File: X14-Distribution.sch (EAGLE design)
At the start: 55 parts, among them Q1 310mA/60V/1.6Ω, Q2 IRF1018EPBF, Q3 IRF1018EPBF, Q4 IRF1018EPBF, Q5 TRANSISTOR-FET_DMP2004K, Q6 TRANSISTOR-FET_DMP2004K, Q7 TRANSISTOR-FET_DMP2004K, U1 DIST_OR_CONTROL_ALTMK06A-M, U2 DIST_OR_CONTROL_ALTMK06A-M

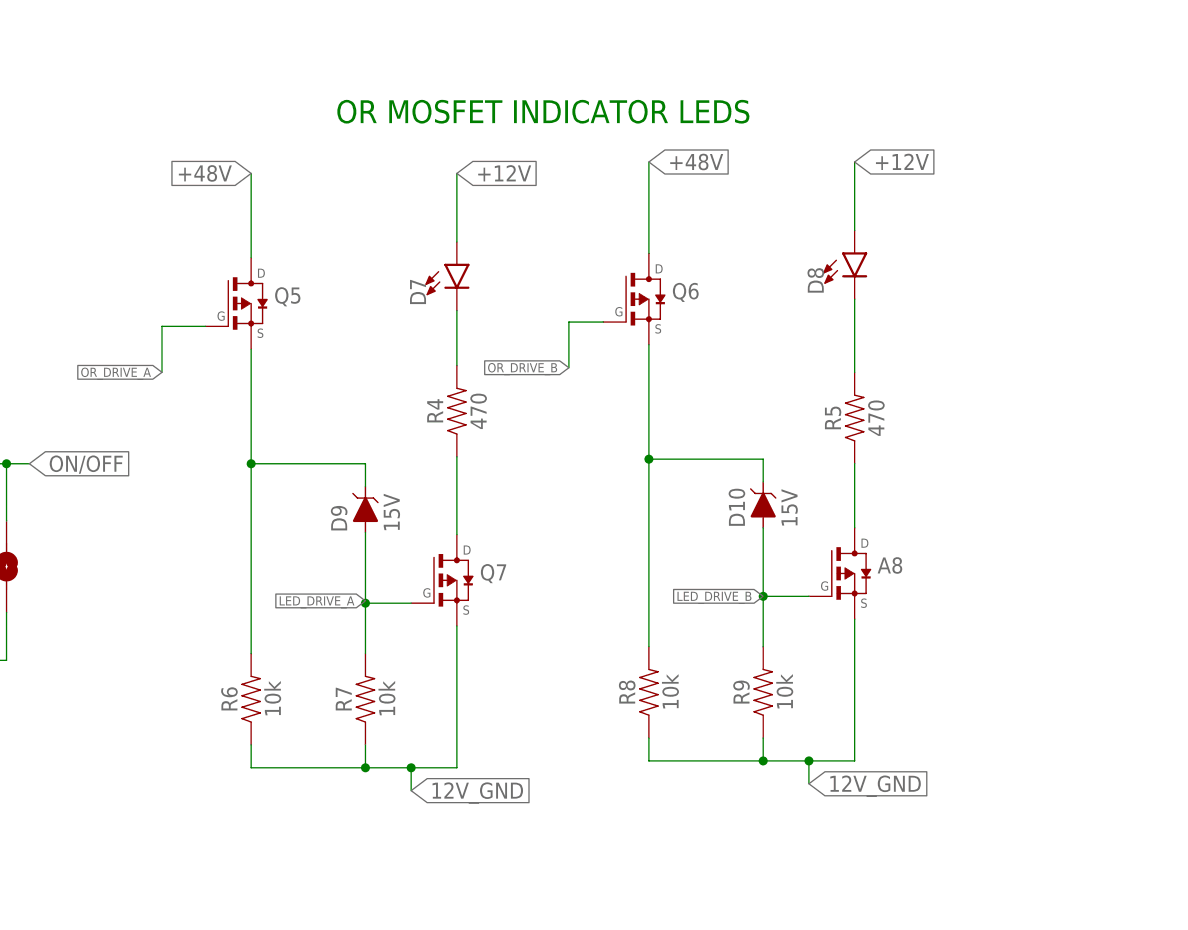
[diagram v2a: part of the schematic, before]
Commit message: Changed the p-mosfets to be oriented the right way
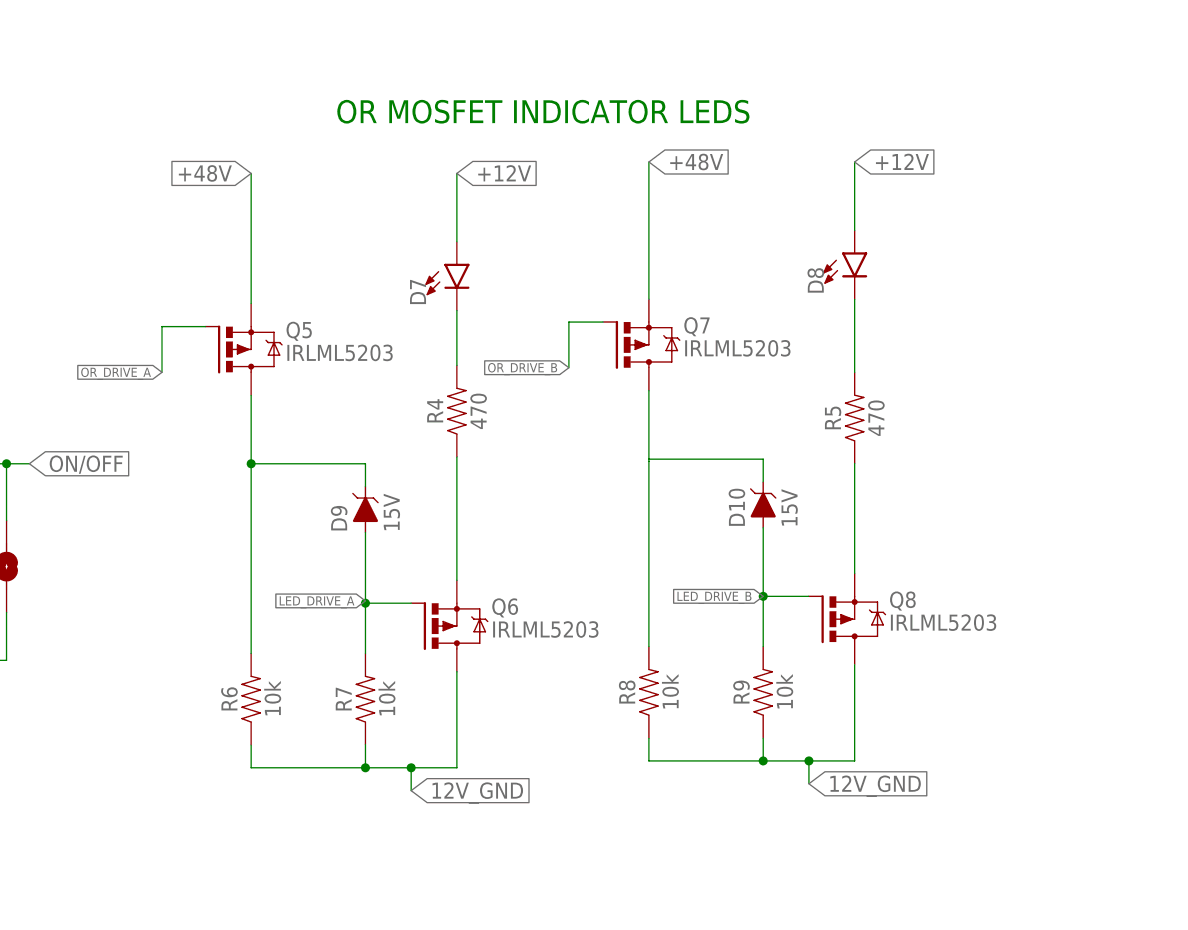
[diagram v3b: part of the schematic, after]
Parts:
- removed A8: TRANSISTOR-FET_DMP2004K, 52101-101-REV-A_v16:TRANSISTOR-FET_DMP2004K
- added Q8: IRLML5203, Transistor:PMOSFET_IRLML5203
- Q5, Q6, Q7: value TRANSISTOR-FET_DMP2004K -> IRLML5203; device 52101-101-REV-A_v16:TRANSISTOR-FET_DMP2004K -> Transistor:PMOSFET_IRLML5203
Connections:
- net +48V: now also Q5.S, Q7.S; no longer Q5.D, Q6.D
- net 12V_GND: now also Q6.D, Q8.D; no longer A8.S, Q7.S
- net LED_DRIVE_A: now also Q6.G; no longer Q7.G
- net LED_DRIVE_B: now also Q8.G; no longer A8.G
- net N$11: now also Q7.D; no longer Q6.S
- net N$3: now also Q6.S; no longer Q7.D
- net N$5: now also Q5.D; no longer Q5.S
- net N$7: now also Q8.S; no longer A8.D
- net OR_DRIVE_B: now also Q7.G; no longer Q6.G
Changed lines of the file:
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@@
 <part name="D11" library="DIODE, Dist Oring Schottky Diode" deviceset="DIODE-DO-214AC(SK34ATR)" device="" value=""/>
 <part name="D12" library="DIODE, Dist Oring Schottky Diode" deviceset="DIODE-DO-214AC(SK34ATR)" device="" value=""/>
-<part name="Q5" library="52101-101-REV-A_v16" library_urn="urn:adsk.eagle:library:21899384" deviceset="TRANSISTOR-FET_DMP2004K" device="" package3d_urn="urn:adsk.eagle:package:15662287/2" value=""/>
-<part name="Q6" library="52101-101-REV-A_v16" library_urn="urn:adsk.eagle:library:21899384" deviceset="TRANSISTOR-FET_DMP2004K" device="" package3d_urn="urn:adsk.eagle:package:15662287/2" value=""/>
-<part name="Q7" library="52101-101-REV-A_v16" library_urn="urn:adsk.eagle:library:21899384" deviceset="TRANSISTOR-FET_DMP2004K" device="" package3d_urn="urn:adsk.eagle:package:15662287/2" value=""/>
-<part name="A8" library="52101-101-REV-A_v16" library_urn="urn:adsk.eagle:library:21899384" deviceset="TRANSISTOR-FET_DMP2004K" device="" package3d_urn="urn:adsk.eagle:package:15662287/2" value=""/>
+<part name="Q5" library="Transistor" library_urn="urn:adsk.eagle:library:16378713" deviceset="PMOSFET_" device="" package3d_urn="urn:adsk.eagle:package:28738/2" technology="IRLML5203" value="IRLML5203"/>
+<part name="Q6" library="Transistor" library_urn="urn:adsk.eagle:library:16378713" deviceset="PMOSFET_" device="" package3d_urn="urn:adsk.eagle:package:28738/2" technology="IRLML5203" value="IRLML5203"/>
+<part name="Q7" library="Transistor" library_urn="urn:adsk.eagle:library:16378713" deviceset="PMOSFET_" device="" package3d_urn="urn:adsk.eagle:package:28738/2" technology="IRLML5203" value="IRLML5203"/>
+<part name="Q8" library="Transistor" library_urn="urn:adsk.eagle:library:16378713" deviceset="PMOSFET_" device="" package3d_urn="urn:adsk.eagle:package:28738/2" technology="IRLML5203" value="IRLML5203"/>
 </parts>
 <sheets>
@@
 <attribute name="VALUE" x="179.07" y="-69.342" size="1.778" layer="96"/>
 </instance>
-<instance part="Q5" gate="G$1" x="190.246" y="116.3574" smashed="yes">
-<attribute name="VALUE" x="192.786" y="113.8174" size="1.778" layer="96"/>
-<attribute name="NAME" x="192.786" y="116.3574" size="1.778" layer="95"/>
-</instance>
-<instance part="Q6" gate="G$1" x="234.442" y="116.84" smashed="yes">
-<attribute name="VALUE" x="236.982" y="114.3" size="1.778" layer="96"/>
-<attribute name="NAME" x="236.982" y="116.84" size="1.778" layer="95"/>
-</instance>
-<instance part="Q7" gate="G$1" x="213.106" y="85.598" smashed="yes">
-<attribute name="VALUE" x="215.646" y="83.058" size="1.778" layer="96"/>
-<attribute name="NAME" x="215.646" y="85.598" size="1.778" layer="95"/>
-</instance>
-<instance part="A8" gate="G$1" x="257.302" y="86.36" smashed="yes">
-<attribute name="VALUE" x="259.842" y="83.82" size="1.778" layer="96"/>
-<attribute name="NAME" x="259.842" y="86.36" size="1.778" layer="95"/>
+<instance part="Q5" gate="G$1" x="187.706" y="111.252" smashed="yes">
+<attribute name="NAME" x="194.056" y="112.522" size="1.778" layer="95"/>
+<attribute name="VALUE" x="194.056" y="109.982" size="1.778" layer="96"/>
+</instance>
+<instance part="Q6" gate="G$1" x="210.566" y="80.518" smashed="yes">
+<attribute name="NAME" x="216.916" y="81.788" size="1.778" layer="95"/>
+<attribute name="VALUE" x="216.916" y="79.248" size="1.778" layer="96"/>
+</instance>
+<instance part="Q7" gate="G$1" x="231.902" y="111.76" smashed="yes">
+<attribute name="NAME" x="238.252" y="113.03" size="1.778" layer="95"/>
+<attribute name="VALUE" x="238.252" y="110.49" size="1.778" layer="96"/>
+</instance>
+<instance part="Q8" gate="G$1" x="254.762" y="81.28" smashed="yes">
+<attribute name="NAME" x="261.112" y="82.55" size="1.778" layer="95"/>
+<attribute name="VALUE" x="261.112" y="80.01" size="1.778" layer="96"/>
 </instance>
 </instances>
@@
 </segment>
 <segment>
-<wire x1="190.246" y1="121.4374" x2="190.246" y2="130.81" width="0.1524" layer="91"/>
 <label x="190.246" y="130.81" size="1.778" layer="95" rot="MR0" xref="yes"/>
-<pinref part="Q5" gate="G$1" pin="D"/>
-</segment>
-<segment>
-<wire x1="234.442" y1="121.92" x2="234.442" y2="132.08" width="0.1524" layer="91"/>
+<pinref part="Q5" gate="G$1" pin="S"/>
+<wire x1="190.246" y1="116.332" x2="190.246" y2="130.81" width="0.1524" layer="91"/>
+</segment>
+<segment>
 <label x="234.442" y="132.08" size="1.778" layer="95" xref="yes"/>
-<pinref part="Q6" gate="G$1" pin="D"/>
+<pinref part="Q7" gate="G$1" pin="S"/>
+<wire x1="234.442" y1="116.84" x2="234.442" y2="132.08" width="0.1524" layer="91"/>
 </segment>
 <segment>
@@
 </segment>
 <segment>
-<wire x1="180.34" y1="113.8174" x2="180.34" y2="108.712" width="0.1524" layer="91"/>
 <label x="180.34" y="108.712" size="1.016" layer="95" rot="R180" xref="yes"/>
 <pinref part="Q5" gate="G$1" pin="G"/>
-<wire x1="180.34" y1="113.8174" x2="185.166" y2="113.8174" width="0.1524" layer="91"/>
+<wire x1="180.34" y1="113.792" x2="180.34" y2="108.712" width="0.1524" layer="91"/>
+<wire x1="180.34" y1="113.792" x2="185.166" y2="113.792" width="0.1524" layer="91"/>
 </segment>
 </net>
@@
 <wire x1="225.552" y1="114.3" x2="225.552" y2="109.22" width="0.1524" layer="91"/>
 <label x="225.552" y="109.22" size="1.016" layer="95" rot="R180" xref="yes"/>
-<pinref part="Q6" gate="G$1" pin="G"/>
+<pinref part="Q7" gate="G$1" pin="G"/>
 <wire x1="225.552" y1="114.3" x2="229.362" y2="114.3" width="0.1524" layer="91"/>
 </segment>
@@
 <junction x="208.026" y="64.77"/>
 <label x="208.026" y="62.23" size="1.778" layer="95" xref="yes"/>
-<pinref part="Q7" gate="G$1" pin="S"/>
-<wire x1="213.106" y1="64.77" x2="213.106" y2="80.518" width="0.1524" layer="91"/>
+<pinref part="Q6" gate="G$1" pin="D"/>
+<wire x1="213.106" y1="64.77" x2="213.106" y2="75.438" width="0.1524" layer="91"/>
 </segment>
 <segment>
@@
 <junction x="252.222" y="65.532"/>
 <label x="252.222" y="62.992" size="1.778" layer="95" xref="yes"/>
-<pinref part="A8" gate="G$1" pin="S"/>
-<wire x1="257.302" y1="65.532" x2="257.302" y2="81.28" width="0.1524" layer="91"/>
+<pinref part="Q8" gate="G$1" pin="D"/>
+<wire x1="257.302" y1="65.532" x2="257.302" y2="76.2" width="0.1524" layer="91"/>
 </segment>
 <segment>
@@
 <wire x1="202.946" y1="96.012" x2="202.946" y2="98.552" width="0.1524" layer="91"/>
 <wire x1="202.946" y1="98.552" x2="190.246" y2="98.552" width="0.1524" layer="91"/>
-<pinref part="Q5" gate="G$1" pin="S"/>
-<wire x1="190.246" y1="111.2774" x2="190.246" y2="98.552" width="0.1524" layer="91"/>
 <junction x="190.246" y="98.552"/>
+<pinref part="Q5" gate="G$1" pin="D"/>
+<wire x1="190.246" y1="106.172" x2="190.246" y2="98.552" width="0.1524" layer="91"/>
 </segment>
 </net>
@@
 <label x="202.946" y="83.312" size="1.016" layer="95" rot="R180" xref="yes"/>
 <wire x1="202.946" y1="77.47" x2="202.946" y2="83.058" width="0.1524" layer="91"/>
-<pinref part="Q7" gate="G$1" pin="G"/>
 <wire x1="202.946" y1="83.058" x2="202.946" y2="90.932" width="0.1524" layer="91"/>
 <wire x1="202.946" y1="83.058" x2="208.026" y2="83.058" width="0.1524" layer="91"/>
 <junction x="202.946" y="83.058"/>
+<pinref part="Q6" gate="G$1" pin="G"/>
 </segment>
 </net>
@@
 <pinref part="R8" gate="G$1" pin="2"/>
 <pinref part="D10" gate="G$1" pin="C"/>
-<wire x1="234.442" y1="99.06" x2="234.442" y2="78.232" width="0.1524" layer="91"/>
+<wire x1="234.442" y1="99.06" x2="234.442" y2="98.806" width="0.1524" layer="91"/>
+<wire x1="234.442" y1="98.806" x2="234.442" y2="78.232" width="0.1524" layer="91"/>
 <wire x1="247.142" y1="96.52" x2="247.142" y2="99.06" width="0.1524" layer="91"/>
 <wire x1="247.142" y1="99.06" x2="234.442" y2="99.06" width="0.1524" layer="91"/>
-<pinref part="Q6" gate="G$1" pin="S"/>
-<wire x1="234.442" y1="99.06" x2="234.442" y2="111.76" width="0.1524" layer="91"/>
-<junction x="234.442" y="99.06"/>
+<pinref part="Q7" gate="G$1" pin="D"/>
+<wire x1="234.442" y1="99.06" x2="234.442" y2="106.68" width="0.1524" layer="91"/>
 </segment>
 </net>
@@
 <pinref part="R9" gate="G$1" pin="2"/>
 <pinref part="D10" gate="G$1" pin="A"/>
+<label x="247.142" y="83.82" size="1.016" layer="95" rot="R180" xref="yes"/>
 <wire x1="247.142" y1="78.232" x2="247.142" y2="83.82" width="0.1524" layer="91"/>
-<label x="247.142" y="83.82" size="1.016" layer="95" rot="R180" xref="yes"/>
-<pinref part="A8" gate="G$1" pin="G"/>
+<pinref part="Q8" gate="G$1" pin="G"/>
 <wire x1="247.142" y1="83.82" x2="247.142" y2="91.44" width="0.1524" layer="91"/>
 <wire x1="247.142" y1="83.82" x2="252.222" y2="83.82" width="0.1524" layer="91"/>
@@
 <segment>
 <pinref part="R4" gate="G$1" pin="1"/>
-<pinref part="Q7" gate="G$1" pin="D"/>
-<wire x1="213.106" y1="99.314" x2="213.106" y2="90.678" width="0.1524" layer="91"/>
+<pinref part="Q6" gate="G$1" pin="S"/>
+<wire x1="213.106" y1="99.314" x2="213.106" y2="85.598" width="0.1524" layer="91"/>
 </segment>
 </net>
 <net name="N$7" class="0">
 <segment>
-<pinref part="A8" gate="G$1" pin="D"/>
+<pinref part="Q8" gate="G$1" pin="S"/>
 <pinref part="R5" gate="G$1" pin="1"/>
-<wire x1="257.302" y1="91.44" x2="257.302" y2="98.552" width="0.1524" layer="91"/>
-</segment>
-</net>
+<wire x1="257.302" y1="86.36" x2="257.302" y2="98.552" width="0.1524" layer="91"/>
+</segment>
+</net>
